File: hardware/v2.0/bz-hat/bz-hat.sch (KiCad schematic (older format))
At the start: 33 parts, among them J1 LineOUT, J2 Headphones, J3 LineIN, U1 WM8731

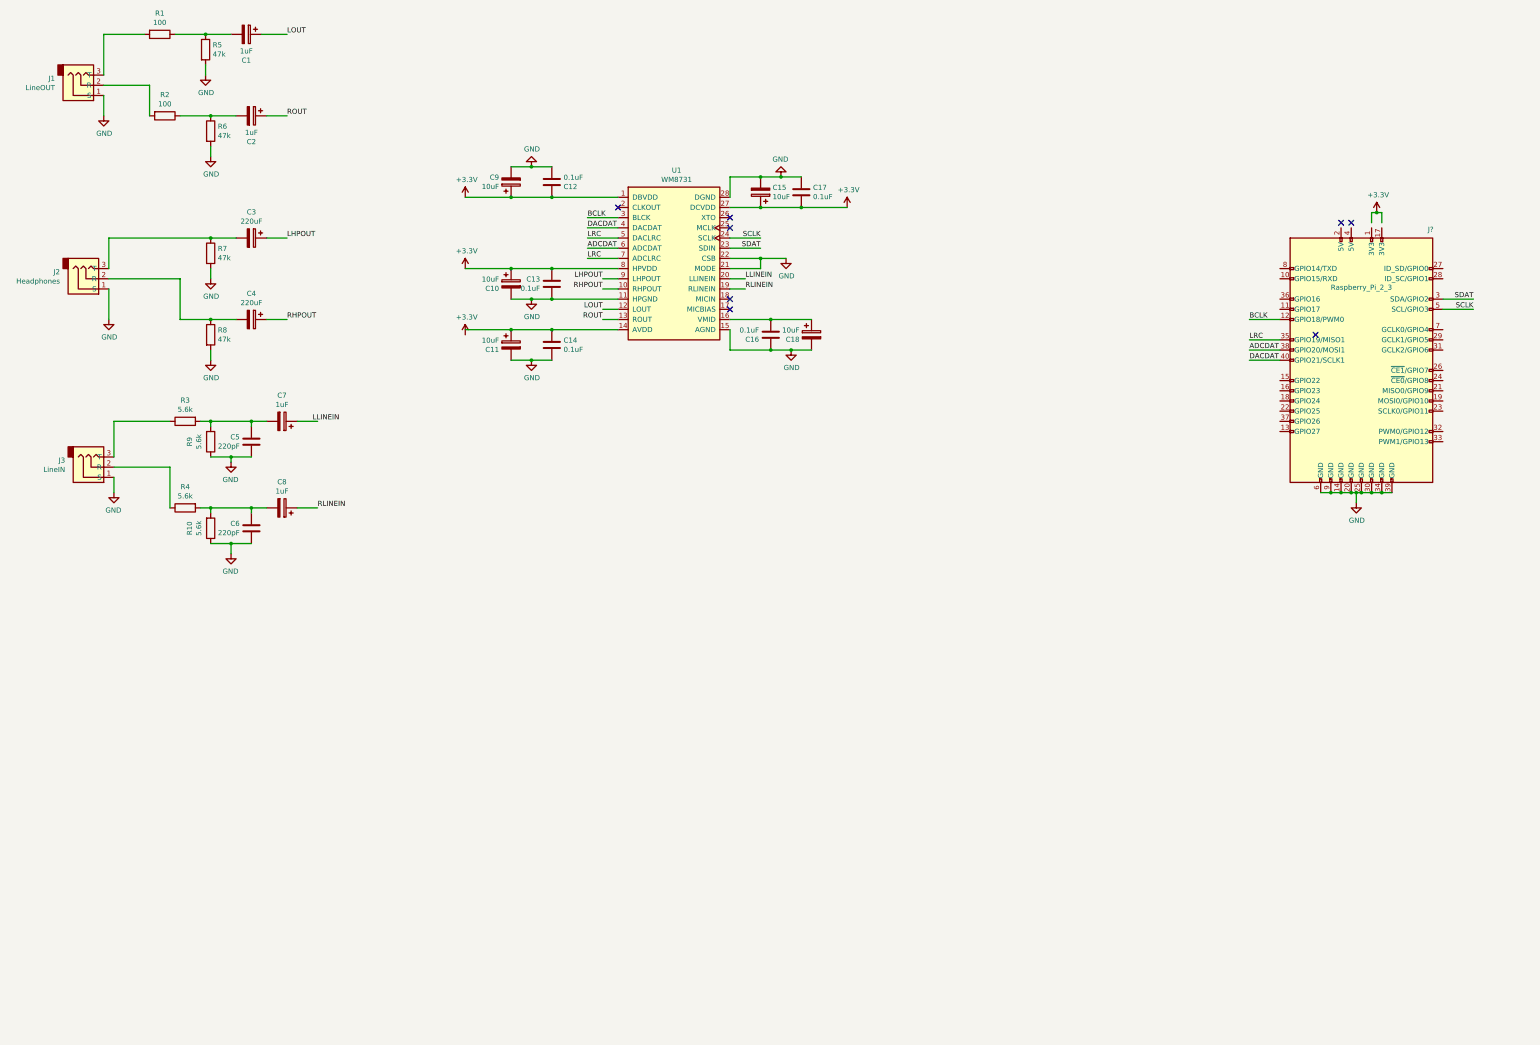
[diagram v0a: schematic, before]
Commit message: KiCAD - raspberrypi 4 symbol and MCP3004s added
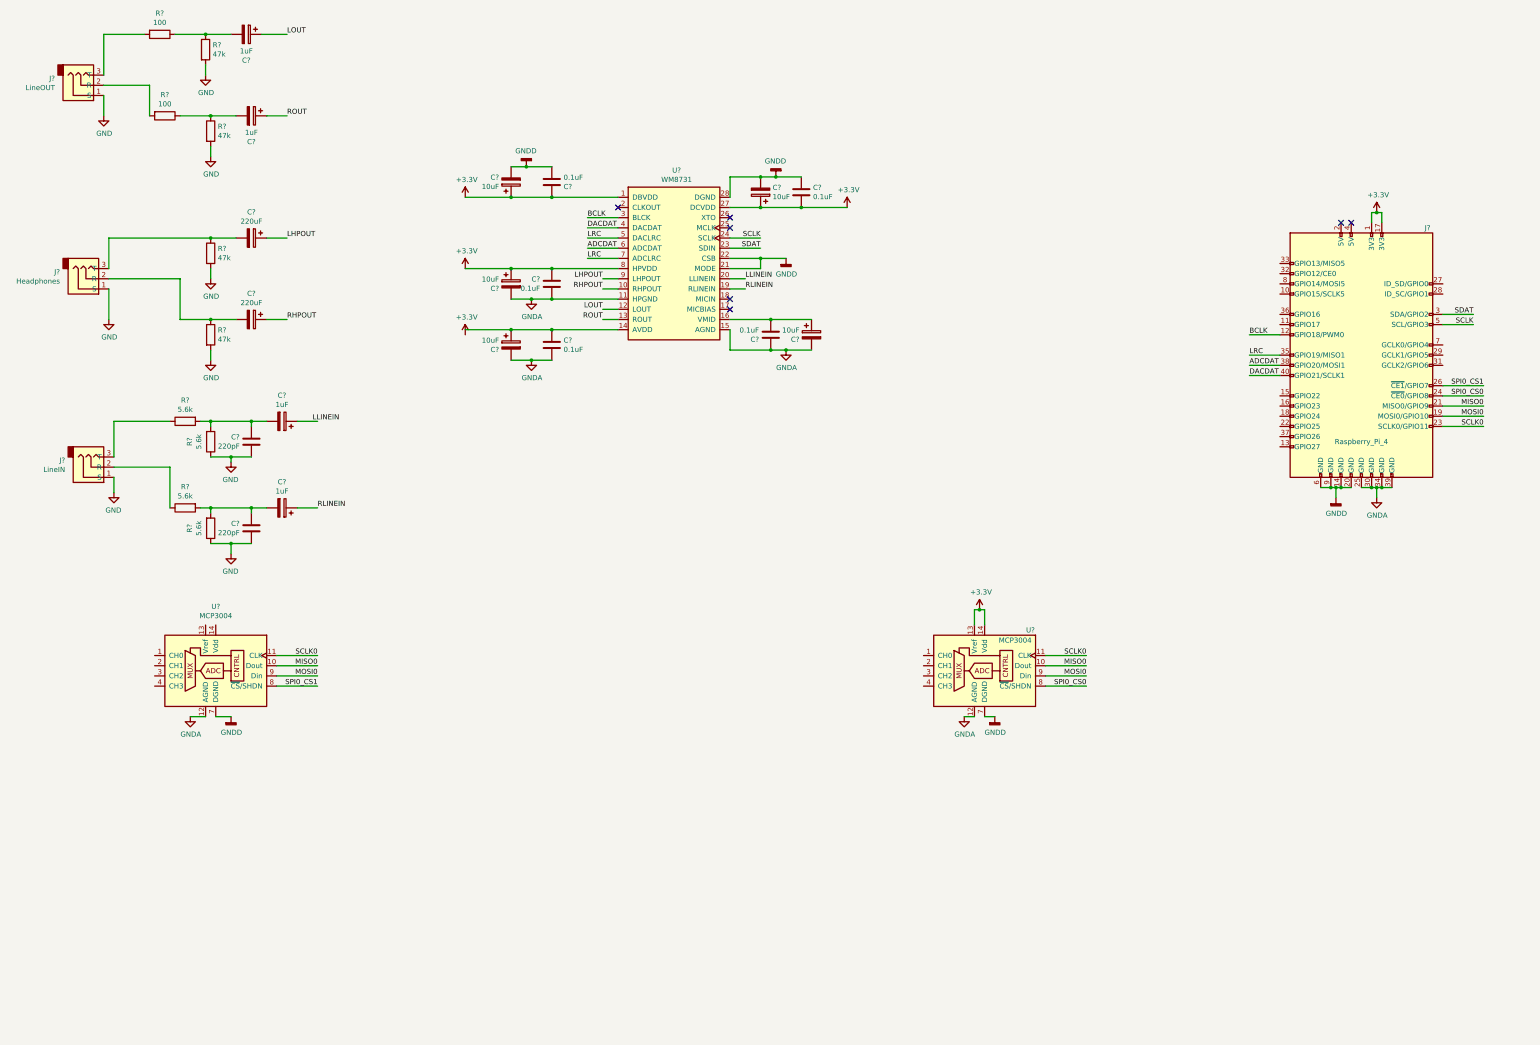
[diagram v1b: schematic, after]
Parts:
- removed J?: Raspberry_Pi_2_3, symbol Connector:Raspberry_Pi_2_3
- added J?: Raspberry_Pi_4, symbol Connector:Raspberry_Pi_4
- added U? (x2): MCP3004, symbol Analog_ADC:MCP3004
- renumbered C5 to C?, C7 to C?, C6 to C?, C8 to C?, C1 to C?, C2 to C?, C3 to C?, C4 to C?, C15 to C?, C17 to C?, C18 to C?, C16 to C?, C9 to C?, C12 to C?, C10 to C?, C13 to C?, C11 to C?, C14 to C?, J3 to J?, J1 to J?, J2 to J?, R3 to R?, R9 to R?, R4 to R?, R10 to R?, R5 to R?, R1 to R?, R6 to R?, R2 to R?, R7 to R?, R8 to R?, U1 to U?
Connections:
- net labels added: GNDA, GNDD, MISO0, MOSI0, SCLK0, SPI0_CS0, SPI0_CS1
- wire segments 113 -> 135
- no-connect marks 8 -> 7

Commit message: v2 schematic full draft
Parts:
- added C18: 1u, symbol Device:CP
- added J5: CVs+CLK_connector, symbol Connector_Generic:Conn_01x04
- added J6: NHD-2.23-12832UCB3, symbol Connector_Generic:Conn_01x20
- added RV1, RV2, RV3, RV4: 10k, symbol Device:R_POT
- added SW1: BTN_f, symbol Switch:SW_Push
- added SW2: BTN_big, symbol Switch:SW_Push
- added SW3: BTN_1, symbol Switch:SW_Push
- added SW4: BTN_2, symbol Switch:SW_Push
- added SW5: BTN_3, symbol Switch:SW_Push
- gave numbers to parts that had none: 35
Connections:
- net GND is gone; now on net GNDA: C1.2, C2.2, J1.1 (S), J2.1 (S), J3.1 (S), R10.2, R5.1, R6.1, R7.2, R8.2, R9.2
- net +3V3: now also C11.1, C14.1, U1.13 (Vref), U1.14 (Vdd), U2.14 (AVDD), C18.1, J6.2 (Pin_2), RV1.1, RV2.1, RV3.1, RV4.1
- net GNDA: now also C18.2, RV1.3, RV2.3, RV3.3, RV4.3
- net GNDD: now also J6.1 (Pin_1), J6.10 (Pin_10), J6.11 (Pin_11), J6.12 (Pin_12), J6.13 (Pin_13), J6.14 (Pin_14), J6.19 (Pin_19), J6.20 (Pin_20), J6.5 (Pin_5), J6.6 (Pin_6), SW1.1, SW2.1, SW3.1, SW4.1, SW5.1
- net at U1.1 (CH0): now also J5.1 (Pin_1)
- net at U1.2 (CH1): now also J5.2 (Pin_2)
- net at U1.3 (CH2): now also J5.3 (Pin_3)
- net at U1.4 (CH3): now also J5.4 (Pin_4)
- net CTRL_A: now reaches U3.1 (CH0)
- net CTRL_A: now also RV4.2
- net CTRL_B: now reaches U3.2 (CH1)
- net CTRL_B: now also RV3.2
- net CTRL_C: now reaches U3.3 (CH2)
- net CTRL_C: now also RV2.2
- net CTRL_D: now reaches U3.4 (CH3)
- net CTRL_D: now also RV1.2
- net D_SCLK: now reaches J4.10 (GPIO15/SCLK5)
- net D_SCLK: now also J6.7 (Pin_7)
- net D_RES: now reaches J4.11 (GPIO17)
- net D_RES: now also J6.16 (Pin_16)
- net BTN_f: now reaches J4.15 (GPIO22)
- net BTN_f: now also SW1.2
- net BTN_big: now reaches J4.16 (GPIO23)
- net BTN_big: now also SW2.2
- net BTN_1: now reaches J4.18 (GPIO24)
- net BTN_1: now also SW3.2
- net BTN_2: now reaches J4.22 (GPIO25)
- net BTN_2: now also SW4.2
- net D_CE: now reaches J4.32 (GPIO12/CE0)
- net D_CE: now also J6.17 (Pin_17)
- net D_DC: now reaches J4.36 (GPIO16)
- net D_DC: now also J6.4 (Pin_4)
- net BTN_3: now reaches J4.37 (GPIO26)
- net BTN_3: now also SW5.2
- net D_MOSI: now reaches J4.8 (GPIO14/MOSI5)
- net D_MOSI: now also J6.8 (Pin_8)
- no-connect marks 7 -> 18
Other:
- note added: "Audio Inteface"
- note added: "Controls and display"
- moved on the sheet: C1, C10, C11, C12, C13, C14, C15, C16, C17, C19, C2, C3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

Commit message: Fixed ERC. Full v2 sombrero schematic
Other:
- note added: "Controller: RPI4"
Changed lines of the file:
@@
 encoding utf-8
 Sheet 1 1
-Title ""
+Title "bzzzbz v2 - \"sombrero\" for RPi4"
 Date ""
 Rev ""
@@
 Wire Wire Line
 	4000 9250 3600 9250
-Text Label 4000 9550 2    50   ~ 0
-MOSI0
 Wire Wire Line
 	4000 9550 3600 9550
@@
 Wire Wire Line
 	13950 2400 14350 2400
-Text Label 7650 5350 2    50   ~ 0
-MOSI0
 Wire Wire Line
 	7650 5350 7250 5350
-Text Label 7650 5250 2    50   ~ 0
-MISO0
 Text Label 7650 5150 2    50   ~ 0
 SCLK0
@@
 Wire Wire Line
 	10600 5200 10600 5250
+Text Label 4000 9550 2    50   ~ 0
+MOSI0
+Text Label 7650 5250 2    50   ~ 0
+MISO0
+Text Label 7650 5350 2    50   ~ 0
+MOSI0
+$Comp
+L power:PWR_FLAG #FLG0101
+U 1 1 603FCBE6
+P 4750 7900
+F 0 "#FLG0101" H 4750 7975 50  0001 C CNN
+F 1 "PWR_FLAG" H 4750 8073 50  0000 C CNN
+F 2 "" H 4750 7900 50  0001 C CNN
+F 3 "~" H 4750 7900 50  0001 C CNN
+	1    4750 7900
+	1    0    0    -1
+$EndComp
+$Comp
+L power:PWR_FLAG #FLG0102
+U 1 1 60402265
+P 5200 7900
+F 0 "#FLG0102" H 5200 7975 50  0001 C CNN
+F 1 "PWR_FLAG" H 5200 8073 50  0000 C CNN
+F 2 "" H 5200 7900 50  0001 C CNN
+F 3 "~" H 5200 7900 50  0001 C CNN
+	1    5200 7900
+	1    0    0    -1
+$EndComp
+$Comp
+L power:PWR_FLAG #FLG0103
+U 1 1 6040261F
+P 5650 7900
+F 0 "#FLG0103" H 5650 7975 50  0001 C CNN
+F 1 "PWR_FLAG" H 5650 8073 50  0000 C CNN
+F 2 "" H 5650 7900 50  0001 C CNN
+F 3 "~" H 5650 7900 50  0001 C CNN
+	1    5650 7900
+	1    0    0    -1
+$EndComp
+$Comp
+L power:GNDA #PWR0137
+U 1 1 60402FDF
+P 5650 7900
+F 0 "#PWR0137" H 5650 7650 50  0001 C CNN
+F 1 "GNDA" H 5655 7727 50  0000 C CNN
+F 2 "" H 5650 7900 50  0001 C CNN
+F 3 "" H 5650 7900 50  0001 C CNN
+	1    5650 7900
+	1    0    0    -1
+$EndComp
+$Comp
+L power:GNDD #PWR0138
+U 1 1 60404413
+P 5200 7900
+F 0 "#PWR0138" H 5200 7650 50  0001 C CNN
+F 1 "GNDD" H 5204 7745 50  0000 C CNN
+F 2 "" H 5200 7900 50  0001 C CNN
+F 3 "" H 5200 7900 50  0001 C CNN
+	1    5200 7900
+	1    0    0    -1
+$EndComp
+$Comp
+L power:+3.3V #PWR0139
+U 1 1 604062F7
+P 4750 7900
+F 0 "#PWR0139" H 4750 7750 50  0001 C CNN
+F 1 "+3.3V" H 4765 8073 50  0000 C CNN
+F 2 "" H 4750 7900 50  0001 C CNN
+F 3 "" H 4750 7900 50  0001 C CNN
+	1    4750 7900
+	-1   0    0    1
+$EndComp
+Wire Notes Line
+	900  7300 900  10850
+Wire Notes Line
+	900  10850 6850 10850
+Wire Notes Line
+	6850 10850 6850 7300
+Wire Notes Line
+	6850 7300 900  7300
+Text Notes 6200 10800 0    50   ~ 0
+Controller: RPI4
 $EndSCHEMATC

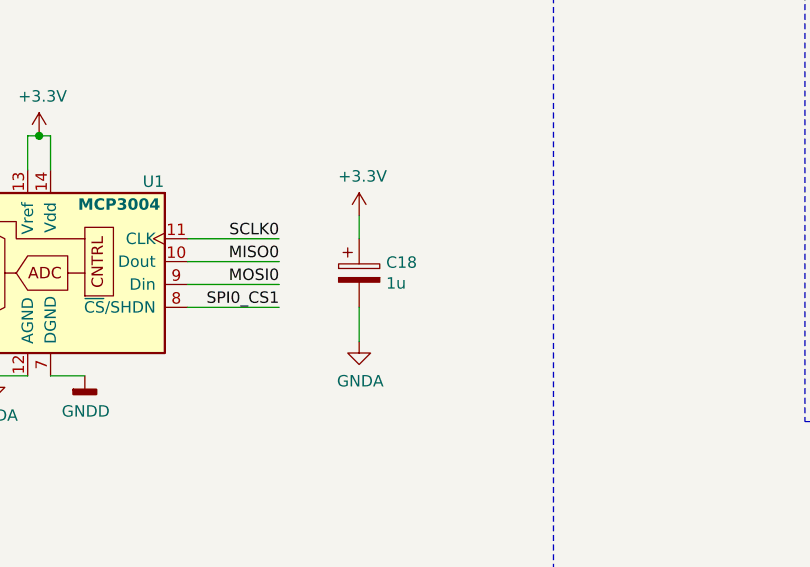
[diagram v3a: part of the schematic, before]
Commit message: big button (PB300) footprint
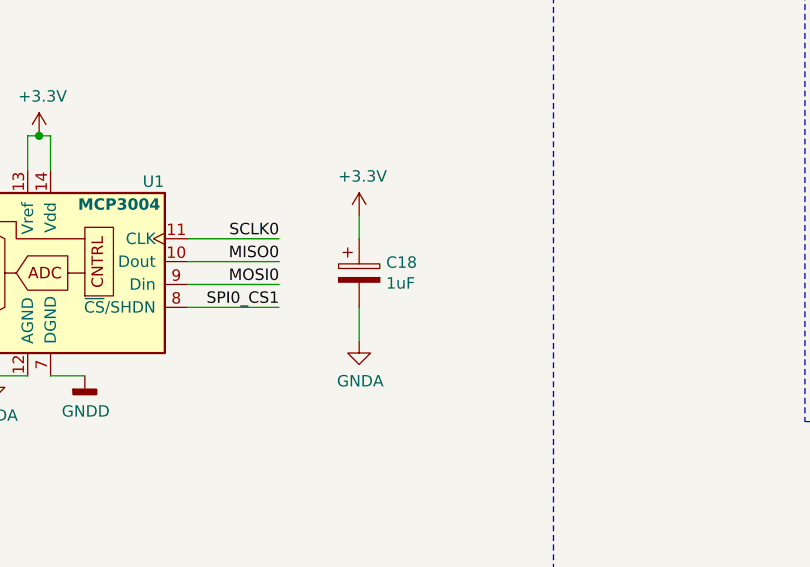
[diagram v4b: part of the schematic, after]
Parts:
- C1, C2: footprint Resistor_THT:R_Axial_DIN0204_L3.6mm_D1.6mm_P2.54mm_Vertical -> Capacitor_SMD:C_0603_1608Metric
- C10, C11, C15, C19, C3, C4, C7, C8, C9: footprint Capacitor_THT:CP_Radial_D5.0mm_P2.00mm -> Capacitor_Tantalum_SMD:CP_EIA-3216-18_Kemet-A
- C12, C13, C14, C16, C17: footprint Resistor_THT:R_Axial_DIN0207_L6.3mm_D2.5mm_P5.08mm_Vertical -> Capacitor_SMD:C_0603_1608Metric
- C18: value 1u -> 1uF; footprint (none) -> Capacitor_SMD:C_0603_1608Metric
- C5, C6: footprint Capacitor_THT:CP_Radial_D10.0mm_P5.00mm -> Capacitor_SMD:CP_Elec_6.3x7.7
- J1, J2, J3: footprint Connector_PinHeader_2.54mm:PinHeader_1x03_P2.54mm_Vertical -> Connector_Audio:Jack_3.5mm_CUI_SJ1-3533NG_Horizontal
- J4: footprint (none) -> Connector_PinHeader_2.54mm:PinHeader_2x20_P2.54mm_Vertical
- J5: footprint (none) -> Connector_PinHeader_2.54mm:PinHeader_1x04_P2.54mm_Vertical
- J6: footprint (none) -> Connector_PinHeader_2.54mm:PinHeader_1x20_P2.54mm_Vertical
- R1, R10, R2, R3, R4, R5, R6, R7, R8, R9: footprint Resistor_THT:R_Axial_DIN0207_L6.3mm_D2.5mm_P7.62mm_Horizontal -> Resistor_SMD:R_0805_2012Metric
- RV1, RV2, RV3, RV4: footprint (none) -> Potentiometer_THT:Potentiometer_Alps_RK09L_Single_Vertical
- SW1, SW3, SW4, SW5: footprint (none) -> Button_Switch_THT:SW_PUSH-12mm
- U1, U3: footprint (none) -> Package_SO:SOIC-14_3.9x8.7mm_P1.27mm
- U2: footprint SOP65P777X199-28N:SOP65P777X199-28N -> bzzzbz:SSOP28-0.65-10.2X5.2MM

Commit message: Fixed footprints and added 3d models
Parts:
- J1, J2, J3: footprint Connector_Audio:Jack_3.5mm_CUI_SJ1-3533NG_Horizontal -> custom:Jack_3.5mm_CUI_SJ1-3533NG_Horizontal
- J6: footprint Connector_PinHeader_2.54mm:PinHeader_1x20_P2.54mm_Vertical -> custom:Display_NHD-2.23-12832
- SW1, SW3, SW4, SW5: footprint Button_Switch_THT:SW_PUSH-12mm -> custom:SW_PUSH-12mm+3d
- SW2: footprint (none) -> custom:SW_PUSH_e-switch_PB300_SPST_12x12
- U2: footprint bzzzbz:SSOP28-0.65-10.2X5.2MM -> custom:SSOP28-0.65-10.2X5.2MM
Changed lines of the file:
@@
 F 0 "U2" H 6775 3715 50  0000 C CNN
 F 1 "WM8731" H 6775 3624 50  0000 C CNB
-F 2 "bzzzbz:SSOP28-0.65-10.2X5.2MM" H 6750 3650 50  0001 C CNN
+F 2 "custom:SSOP28-0.65-10.2X5.2MM" H 6750 3650 50  0001 C CNN
 F 3 "" H 6750 3650 50  0001 C CNN
 	1    6750 2800
@@
 F 0 "J1" H 1271 5483 50  0000 R CNN
 F 1 "LineIN" H 1271 5574 50  0000 R CNB
-F 2 "Connector_Audio:Jack_3.5mm_CUI_SJ1-3533NG_Horizontal" H 1550 5550 50  0001 C CNN
+F 2 "custom:Jack_3.5mm_CUI_SJ1-3533NG_Horizontal" H 1550 5550 50  0001 C CNN
 F 3 "~" H 1550 5550 50  0001 C CNN
 	1    1550 5550
@@
 F 0 "J2" H 1471 2233 50  0000 R CNN
 F 1 "LineOUT" H 1471 2324 50  0000 R CNB
-F 2 "Connector_Audio:Jack_3.5mm_CUI_SJ1-3533NG_Horizontal" H 1750 2300 50  0001 C CNN
+F 2 "custom:Jack_3.5mm_CUI_SJ1-3533NG_Horizontal" H 1750 2300 50  0001 C CNN
 F 3 "~" H 1750 2300 50  0001 C CNN
 	1    1750 2300
@@
 F 0 "J3" H 1520 3783 50  0000 R CNN
 F 1 "Headphones" H 1520 3874 50  0000 R CNB
-F 2 "Connector_Audio:Jack_3.5mm_CUI_SJ1-3533NG_Horizontal" H 1800 3850 50  0001 C CNN
+F 2 "custom:Jack_3.5mm_CUI_SJ1-3533NG_Horizontal" H 1800 3850 50  0001 C CNN
 F 3 "~" H 1800 3850 50  0001 C CNN
 	1    1800 3850
@@
 F 0 "SW1" H 10800 3785 50  0000 C CNN
 F 1 "BTN_f" H 10800 3694 50  0000 C CNN
-F 2 "Button_Switch_THT:SW_PUSH-12mm" H 10800 3700 50  0001 C CNN
+F 2 "custom:SW_PUSH-12mm+3d" H 10800 3700 50  0001 C CNN
 F 3 "~" H 10800 3700 50  0001 C CNN
 	1    10800 3500
@@
 F 0 "SW2" H 10800 4185 50  0000 C CNN
 F 1 "BTN_big" H 10800 4094 50  0000 C CNN
-F 2 "" H 10800 4100 50  0001 C CNN
+F 2 "custom:SW_PUSH_e-switch_PB300_SPST_12x12" H 10800 4100 50  0001 C CNN
 F 3 "~" H 10800 4100 50  0001 C CNN
 	1    10800 3900
@@
 F 0 "SW3" H 10800 4585 50  0000 C CNN
 F 1 "BTN_1" H 10800 4494 50  0000 C CNN
-F 2 "Button_Switch_THT:SW_PUSH-12mm" H 10800 4500 50  0001 C CNN
+F 2 "custom:SW_PUSH-12mm+3d" H 10800 4500 50  0001 C CNN
 F 3 "~" H 10800 4500 50  0001 C CNN
 	1    10800 4300
@@
 F 0 "SW4" H 10800 4985 50  0000 C CNN
 F 1 "BTN_2" H 10800 4894 50  0000 C CNN
-F 2 "Button_Switch_THT:SW_PUSH-12mm" H 10800 4900 50  0001 C CNN
+F 2 "custom:SW_PUSH-12mm+3d" H 10800 4900 50  0001 C CNN
 F 3 "~" H 10800 4900 50  0001 C CNN
 	1    10800 4700
@@
 F 0 "SW5" H 10800 5385 50  0000 C CNN
 F 1 "BTN_3" H 10800 5294 50  0000 C CNN
-F 2 "Button_Switch_THT:SW_PUSH-12mm" H 10800 5300 50  0001 C CNN
+F 2 "custom:SW_PUSH-12mm+3d" H 10800 5300 50  0001 C CNN
 F 3 "~" H 10800 5300 50  0001 C CNN
 	1    10800 5100
@@
 F 0 "J6" H 14100 4150 50  0000 C CNN
 F 1 "NHD-2.23-12832UCB3" H 14500 4050 50  0000 C CNN
-F 2 "Connector_PinHeader_2.54mm:PinHeader_1x20_P2.54mm_Vertical" H 13950 4200 50  0001 C CNN
+F 2 "custom:Display_NHD-2.23-12832" H 13950 4200 50  0001 C CNN
 F 3 "~" H 13950 4200 50  0001 C CNN
 	1    13950 4200

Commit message: v2 board, mounting holes + draft components placement
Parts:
- J4: footprint Connector_PinHeader_2.54mm:PinHeader_2x20_P2.54mm_Vertical -> custom:PinHeader_2x20_P2.54mm_Vertical_RaspberryPI_HAT
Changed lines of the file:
@@
 F 0 "J4" H 3450 10200 50  0000 C CNN
 F 1 "Raspberry_Pi_4" H 2800 8100 50  0000 C CNB
-F 2 "Connector_PinHeader_2.54mm:PinHeader_2x20_P2.54mm_Vertical" H 2800 8950 50  0001 C CNN
+F 2 "custom:PinHeader_2x20_P2.54mm_Vertical_RaspberryPI_HAT" H 2800 8950 50  0001 C CNN
 F 3 "https://www.raspberrypi.org/documentation/hardware/raspberrypi/schematics/rpi_SCH_3bplus_1p0_reduced.pdf" H 2800 8950 50  0001 C CNN
 	1    2800 8950

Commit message: v2 board placement and routing finished
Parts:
- added C20: 1uF, Capacitor_Tantalum_SMD:CP_EIA-3216-18_Kemet-A, symbol Device:CP
- C13: footprint Capacitor_SMD:C_0603_1608Metric -> Capacitor_SMD:C_1206_3216Metric
- C18: footprint Capacitor_SMD:C_0603_1608Metric -> Capacitor_Tantalum_SMD:CP_EIA-3216-18_Kemet-A
- C19: footprint Capacitor_Tantalum_SMD:CP_EIA-3216-18_Kemet-A -> Capacitor_SMD:C_0603_1608Metric
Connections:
- net +3V3: now also C20.1
- net GNDA: now also C20.2
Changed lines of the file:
@@
 F 0 "C19" H 7982 3454 50  0000 R CNN
 F 1 "10uF" H 7982 3545 50  0000 R CNN
-F 2 "Capacitor_Tantalum_SMD:CP_EIA-3216-18_Kemet-A" H 8138 3350 50  0001 C CNN
+F 2 "Capacitor_SMD:C_0603_1608Metric" H 8138 3350 50  0001 C CNN
 F 3 "~" H 8100 3500 50  0001 C CNN
 	1    8100 3500
@@
 F 0 "C13" H 5665 3046 50  0000 L CNN
 F 1 "0.1uF" H 5665 2955 50  0000 L CNN
-F 2 "Capacitor_SMD:C_0603_1608Metric" H 5588 2850 50  0001 C CNN
+F 2 "Capacitor_SMD:C_1206_3216Metric" H 5588 2850 50  0001 C CNN
 F 3 "~" H 5550 3000 50  0001 C CNN
 	1    5550 3000
@@
 F 0 "C18" H 8118 5346 50  0000 L CNN
 F 1 "1uF" H 8118 5255 50  0000 L CNN
-F 2 "Capacitor_SMD:C_0603_1608Metric" H 8038 5150 50  0001 C CNN
+F 2 "Capacitor_Tantalum_SMD:CP_EIA-3216-18_Kemet-A" H 8038 5150 50  0001 C CNN
 F 3 "~" H 8000 5300 50  0001 C CNN
 	1    8000 5300
@@
 Text Notes 6200 10800 0    50   ~ 0
 Controller: RPI4
+$Comp
+L Device:CP C20
+U 1 1 6049D16C
+P 14700 2200
+F 0 "C20" H 14818 2246 50  0000 L CNN
+F 1 "1uF" H 14818 2155 50  0000 L CNN
+F 2 "Capacitor_Tantalum_SMD:CP_EIA-3216-18_Kemet-A" H 14738 2050 50  0001 C CNN
+F 3 "~" H 14700 2200 50  0001 C CNN
+	1    14700 2200
+	1    0    0    -1
+$EndComp
+$Comp
+L power:+3.3V #PWR03
+U 1 1 6049D172
+P 14700 1950
+F 0 "#PWR03" H 14700 1800 50  0001 C CNN
+F 1 "+3.3V" H 14715 2123 50  0000 C CNN
+F 2 "" H 14700 1950 50  0001 C CNN
+F 3 "" H 14700 1950 50  0001 C CNN
+	1    14700 1950
+	1    0    0    -1
+$EndComp
+$Comp
+L power:GNDA #PWR04
+U 1 1 6049D178
+P 14700 2500
+F 0 "#PWR04" H 14700 2250 50  0001 C CNN
+F 1 "GNDA" H 14705 2327 50  0000 C CNN
+F 2 "" H 14700 2500 50  0001 C CNN
+F 3 "" H 14700 2500 50  0001 C CNN
+	1    14700 2500
+	1    0    0    -1
+$EndComp
+Wire Wire Line
+	14700 1950 14700 2050
+Wire Wire Line
+	14700 2350 14700 2500
 $EndSCHEMATC
